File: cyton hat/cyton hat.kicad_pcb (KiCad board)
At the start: 4 copper layers, 61.4 x 61.3 mm, 59 parts, among them J1 Conn_02x13_Odd_Even, J2 Conn_01x08, J3 Conn_01x04, J4 Conn_01x02, J5 Conn_01x04, U1 ADS129x, U2 CP2102N-Axx-xQFN24

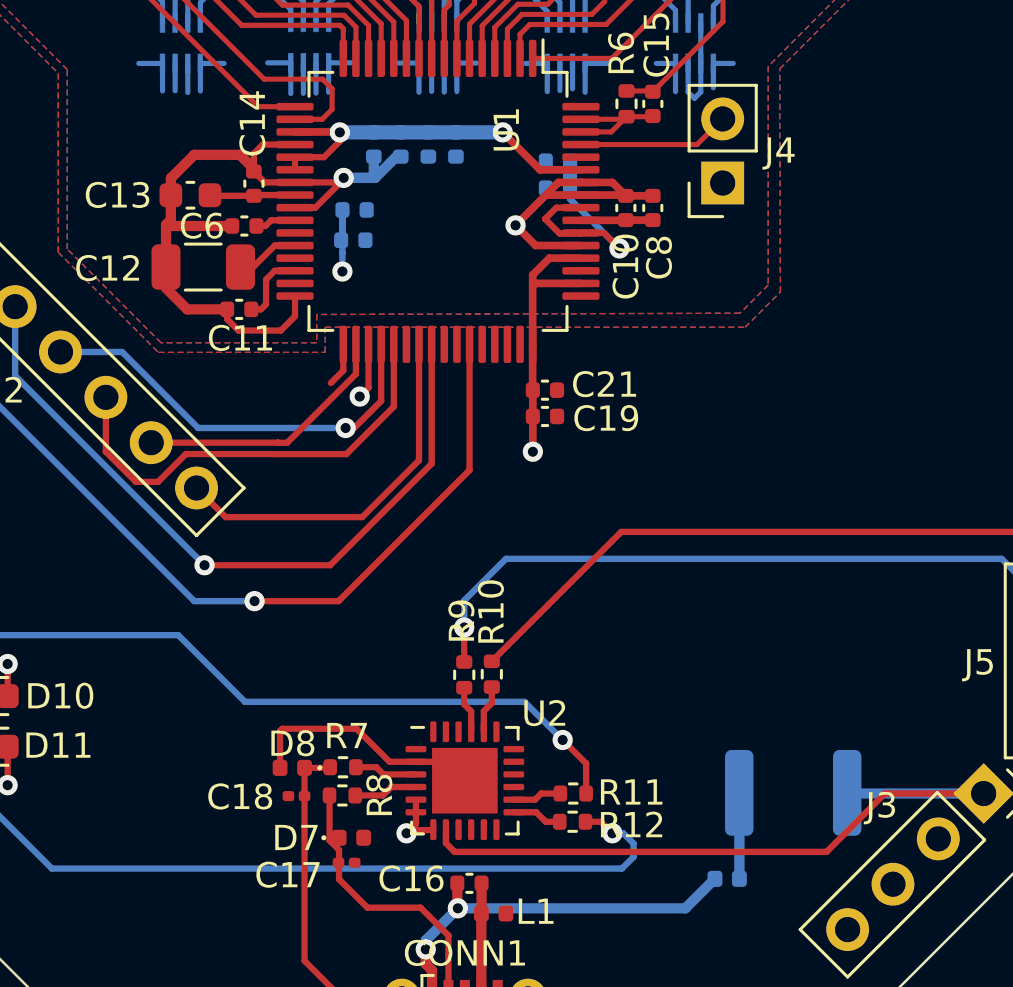
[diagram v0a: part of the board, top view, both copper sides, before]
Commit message: moved via that missed VSSA plane
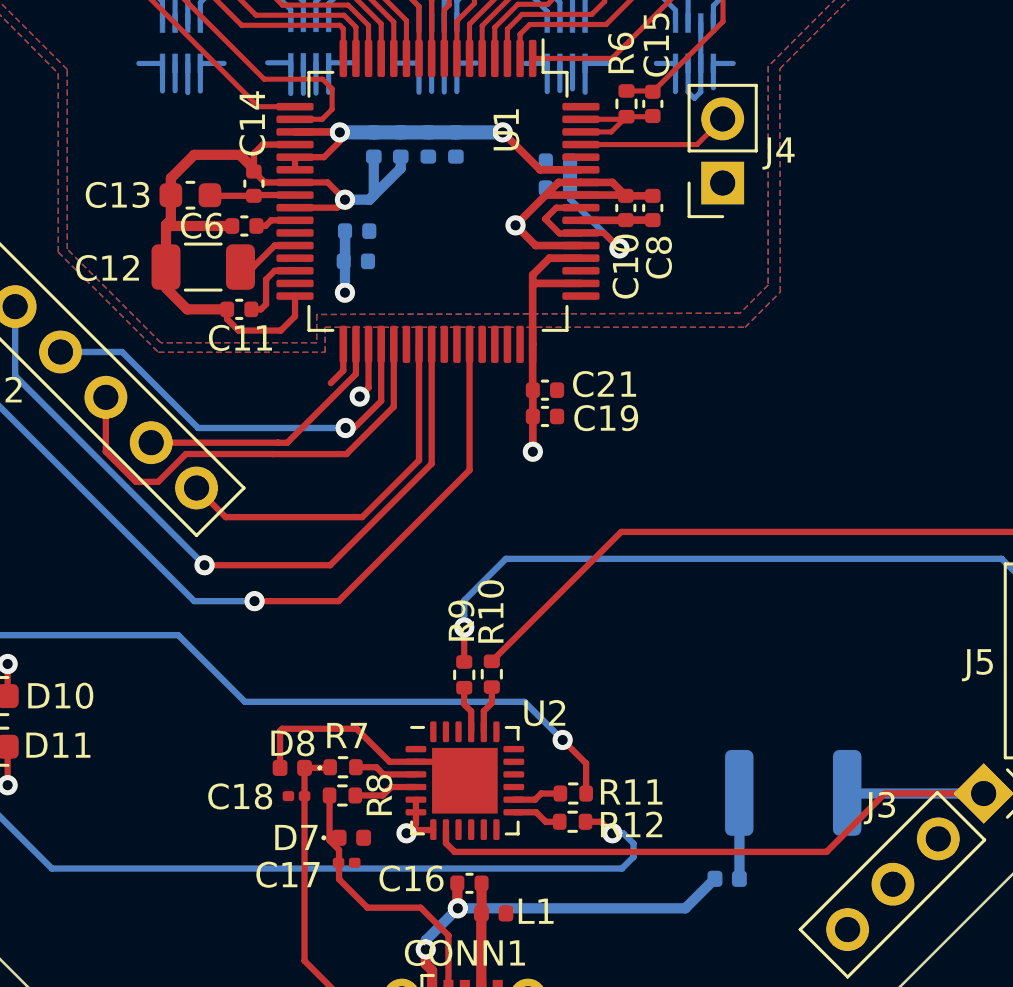
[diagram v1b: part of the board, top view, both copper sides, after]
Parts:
- moved C9 0.84 mm to (135.4, 104.2)
- moved C7 0.84 mm to (135.4, 103.0)
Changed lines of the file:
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@@
       (outputformat 1)
       (mirror false)
-      (drillshape 1)
+      (drillshape 0)
       (scaleselection 1)
-      (outputdirectory "")
+      (outputdirectory "plots/")
     )
   )
@@
     (fp_line (start -2 -1) (end -1 -2) (layer "F.Fab") (width 0.1))
     (fp_line (start -2 2) (end -2 -1) (layer "F.Fab") (width 0.1))
-    (pad "" smd roundrect (at 0.65 -0.65) (size 1.05 1.05) (layers "F.Paste") (roundrect_rratio 0.238095))
-    (pad "" smd roundrect (at -0.65 -0.65) (size 1.05 1.05) (layers "F.Paste") (roundrect_rratio 0.238095))
-    (pad "" smd roundrect (at -0.65 0.65) (size 1.05 1.05) (layers "F.Paste") (roundrect_rratio 0.238095))
-    (pad "" smd roundrect (at 0.65 0.65) (size 1.05 1.05) (layers "F.Paste") (roundrect_rratio 0.238095))
+    (pad "" smd roundrect (at 0.65 -0.65) (size 1.05 1.05) (layers "F.Paste") (roundrect_rratio 0.2380952381))
+    (pad "" smd roundrect (at -0.65 -0.65) (size 1.05 1.05) (layers "F.Paste") (roundrect_rratio 0.2380952381))
+    (pad "" smd roundrect (at -0.65 0.65) (size 1.05 1.05) (layers "F.Paste") (roundrect_rratio 0.2380952381))
+    (pad "" smd roundrect (at 0.65 0.65) (size 1.05 1.05) (layers "F.Paste") (roundrect_rratio 0.2380952381))
     (pad "1" smd roundrect (at -1.9375 -1.25) (size 0.825 0.25) (layers "F.Cu" "F.Paste" "F.Mask") (roundrect_rratio 0.25)
       (net 91 "unconnected-(U2-Pad1)") (pinfunction "~{RI}/CLK") (pintype "bidirectional+no_connect"))
@@
     (fp_line (start 1.6 0.8) (end -1.6 0.8) (layer "F.Fab") (width 0.1))
     (fp_line (start 1.6 -0.8) (end 1.6 0.8) (layer "F.Fab") (width 0.1))
-    (pad "1" smd roundrect (at -1.475 0) (size 1.15 1.8) (layers "F.Cu" "F.Paste" "F.Mask") (roundrect_rratio 0.217391)
+    (pad "1" smd roundrect (at -1.475 0) (size 1.15 1.8) (layers "F.Cu" "F.Paste" "F.Mask") (roundrect_rratio 0.2173913043)
       (net 21 "VSSA") (pintype "passive"))
-    (pad "2" smd roundrect (at 1.475 0) (size 1.15 1.8) (layers "F.Cu" "F.Paste" "F.Mask") (roundrect_rratio 0.217391)
+    (pad "2" smd roundrect (at 1.475 0) (size 1.15 1.8) (layers "F.Cu" "F.Paste" "F.Mask") (roundrect_rratio 0.2173913043)
       (net 25 "Net-(C12-Pad2)") (pintype "passive"))
     (model "${KICAD6_3DMODEL_DIR}/Capacitor_SMD.3dshapes/C_1206_3216Metric.wrl"
@@
     (fp_line (start -2.25 1.6) (end 2.25 1.6) (layer "B.Fab") (width 0.1))
     (fp_line (start 2.25 1.6) (end 2.25 -1.6) (layer "B.Fab") (width 0.1))
-    (pad "1" smd roundrect (at -2.1375 0 180) (size 1.125 3.4) (layers "B.Cu" "B.Paste" "B.Mask") (roundrect_rratio 0.222222)
+    (pad "1" smd roundrect (at -2.1375 0 180) (size 1.125 3.4) (layers "B.Cu" "B.Paste" "B.Mask") (roundrect_rratio 0.2222222222)
       (net 63 "VCOM") (pintype "passive"))
-    (pad "2" smd roundrect (at 2.1375 0 180) (size 1.125 3.4) (layers "B.Cu" "B.Paste" "B.Mask") (roundrect_rratio 0.222222)
+    (pad "2" smd roundrect (at 2.1375 0 180) (size 1.125 3.4) (layers "B.Cu" "B.Paste" "B.Mask") (roundrect_rratio 0.2222222222)
       (net 64 "Net-(F1-Pad2)") (pintype "passive"))
     (model "${KICAD6_3DMODEL_DIR}/Fuse.3dshapes/Fuse_1812_4532Metric.wrl"
@@
   )
   (footprint "Capacitor_SMD:C_0402_1005Metric" (layer "B.Cu")
-    (at 135.2804 103.406)
+    (at 135.382 104.2442)
     (descr "Capacitor SMD 0402 (1005 Metric), square (rectangular) end terminal, IPC_7351 nominal, (Body size source: IPC-SM-782 page 76, https://www.pcb-3d.com/wordpress/wp-content/uploads/ipc-sm-782a_amendment_1_and_2.pdf), generated with kicad-footprint-generator")
     (tags "capacitor")
@@
   )
   (footprint "Capacitor_SMD:C_0402_1005Metric" (layer "B.Cu")
-    (at 135.3312 102.2096)
+    (at 135.4328 103.0478)
     (descr "Capacitor SMD 0402 (1005 Metric), square (rectangular) end terminal, IPC_7351 nominal, (Body size source: IPC-SM-782 page 76, https://www.pcb-3d.com/wordpress/wp-content/uploads/ipc-sm-782a_amendment_1_and_2.pdf), generated with kicad-footprint-generator")
     (tags "capacitor")
@@
   (segment (start 131.699 99.6188) (end 131.3434 99.9744) (width 0.254) (layer "F.Cu") (net 21))
   (segment (start 145.5434 101.1188) (end 146.0754 101.6508) (width 0.3048) (layer "F.Cu") (net 21))
+  (segment (start 134.9502 101.8032) (end 134.6346 102.1188) (width 0.25) (layer "F.Cu") (net 21))
   (segment (start 146.0754 101.6508) (end 147.1422 101.6508) (width 0.3048) (layer "F.Cu") (net 21))
   (segment (start 127.915 102.8446) (end 127.8636 102.7932) (width 0.25) (layer "F.Cu") (net 21))
   (segment (start 128.0538 100.9526) (end 128.0538 101.6254) (width 0.4064) (layer "F.Cu") (net 21))
-  (segment (start 134.8994 100.994985) (end 133.775585 102.1188) (width 0.25) (layer "F.Cu") (net 21))
   (segment (start 144.2974 101.6188) (end 146.0434 101.6188) (width 0.3048) (layer "F.Cu") (net 21))
   (segment (start 146.0434 101.6188) (end 146.0754 101.6508) (width 0.2032) (layer "F.Cu") (net 21))
@@
   (segment (start 131.3434 99.9744) (end 131.3434 100.6882) (width 0.254) (layer "F.Cu") (net 21))
   (segment (start 131.774 101.1188) (end 131.3434 100.6882) (width 0.254) (layer "F.Cu") (net 21))
-  (segment (start 134.8994 100.9396) (end 134.7202 101.1188) (width 0.25) (layer "F.Cu") (net 21))
-  (segment (start 134.7202 101.1188) (end 132.9724 101.1188) (width 0.25) (layer "F.Cu") (net 21))
   (segment (start 128.0538 101.6254) (end 128.0538 102.603) (width 0.4064) (layer "F.Cu") (net 21))
   (segment (start 130.2818 106.5328) (end 130.2818 106.1466) (width 0.25) (layer "F.Cu") (net 21))
-  (segment (start 133.775585 102.1188) (end 132.9724 102.1188) (width 0.25) (layer "F.Cu") (net 21))
+  (segment (start 134.9502 101.8032) (end 134.2658 101.1188) (width 0.25) (layer "F.Cu") (net 21))
   (segment (start 132.9724 101.1188) (end 131.774 101.1188) (width 0.254) (layer "F.Cu") (net 21))
   (segment (start 127.8636 104.4684) (end 127.8618 104.4702) (width 0.25) (layer "F.Cu") (net 21))
@@
   (segment (start 144.2974 101.6188) (end 142.9192 101.6188) (width 0.3048) (layer "F.Cu") (net 21))
   (segment (start 143.407 101.1188) (end 142.9131 101.6127) (width 0.3048) (layer "F.Cu") (net 21))
-  (segment (start 134.8994 100.9396) (end 134.8994 100.994985) (width 0.25) (layer "F.Cu") (net 21))
+  (segment (start 134.2658 101.1188) (end 132.9724 101.1188) (width 0.25) (layer "F.Cu") (net 21))
+  (segment (start 134.6346 102.1188) (end 132.9724 102.1188) (width 0.25) (layer "F.Cu") (net 21))
   (segment (start 142.5062 103.6188) (end 141.7066 102.8192) (width 0.3048) (layer "F.Cu") (net 21))
   (segment (start 130.7846 100.0252) (end 128.9812 100.0252) (width 0.4064) (layer "F.Cu") (net 21))
@@
   (segment (start 127.8636 102.7932) (end 127.8636 104.4684) (width 0.4064) (layer "F.Cu") (net 21))
   (segment (start 132.9724 105.6188) (end 132.9724 106.4226) (width 0.25) (layer "F.Cu") (net 21))
-  (via (at 134.8994 100.9396) (size 0.8) (drill 0.4) (layers "F.Cu" "B.Cu") (net 21))
-  (via (at 134.8486 104.648) (size 0.8) (drill 0.4) (layers "F.Cu" "B.Cu") (free) (net 21))
+  (via (at 134.9502 101.8032) (size 0.8) (drill 0.4) (layers "F.Cu" "B.Cu") (net 21))
+  (via (at 134.9502 105.4862) (size 0.8) (drill 0.4) (layers "F.Cu" "B.Cu") (free) (net 21))
   (via (at 141.7066 102.8192) (size 0.8) (drill 0.4) (layers "F.Cu" "B.Cu") (net 21))
-  (segment (start 134.8486 104.648) (end 134.8486 103.9042) (width 0.25) (layer "B.Cu") (net 21))
-  (segment (start 134.8512 103.9016) (end 134.8512 102.2096) (width 0.25) (layer "B.Cu") (net 21))
-  (segment (start 134.8486 103.9042) (end 134.8512 103.9016) (width 0.25) (layer "B.Cu") (net 21))
+  (segment (start 134.9502 105.4862) (end 134.9502 104.7424) (width 0.4064) (layer "B.Cu") (net 21))
+  (segment (start 135.9154 101.8032) (end 137.16 100.5586) (width 0.4064) (layer "B.Cu") (net 21))
+  (segment (start 136.0932 100.0962) (end 136.0932 101.6254) (width 0.4064) (layer "B.Cu") (net 21))
+  (segment (start 137.16 100.5586) (end 137.16 100.0962) (width 0.4064) (layer "B.Cu") (net 21))
+  (segment (start 134.9528 104.7398) (end 134.9528 103.0478) (width 0.4064) (layer "B.Cu") (net 21))
+  (segment (start 134.9502 104.7424) (end 134.9528 104.7398) (width 0.25) (layer "B.Cu") (net 21))
   (segment (start 126.176799 89.143599) (end 127.33655 89.143599) (width 0.2032) (layer "B.Cu") (net 21))
-  (segment (start 137.16 100.0962) (end 136.9874 100.0962) (width 0.25) (layer "B.Cu") (net 21))
-  (segment (start 136.0932 100.0962) (end 136.0932 100.7618) (width 0.4064) (layer "B.Cu") (net 21))
-  (segment (start 136.144 100.9396) (end 134.8994 100.9396) (width 0.4064) (layer "B.Cu") (net 21))
-  (segment (start 134.8512 103.3552) (end 134.8004 103.406) (width 0.25) (layer "B.Cu") (net 21))
+  (segment (start 134.9528 104.1934) (end 134.902 104.2442) (width 0.25) (layer "B.Cu") (net 21))
   (segment (start 124.6632 84.9884) (end 124.6632 87.63) (width 0.2032) (layer "B.Cu") (net 21))
-  (segment (start 136.0932 100.7618) (end 135.9154 100.9396) (width 0.25) (layer "B.Cu") (net 21))
-  (segment (start 135.9154 100.9396) (end 134.8994 100.9396) (width 0.4064) (layer "B.Cu") (net 21))
-  (segment (start 136.9874 100.0962) (end 136.144 100.9396) (width 0.4064) (layer "B.Cu") (net 21))
+  (segment (start 134.9502 101.8032) (end 135.9154 101.8032) (width 0.4064) (layer "B.Cu") (net 21))
+  (segment (start 136.0932 101.6254) (end 135.9154 101.8032) (width 0.4064) (layer "B.Cu") (net 21))
   (segment (start 124.6632 87.63) (end 126.176799 89.143599) (width 0.2032) (layer "B.Cu") (net 21))
-  (segment (start 134.8512 102.2096) (end 134.8512 103.3552) (width 0.25) (layer "B.Cu") (net 21))
+  (segment (start 134.9528 103.0478) (end 134.9528 104.1934) (width 0.4064) (layer "B.Cu") (net 21))
   (segment (start 132.0264 102.6188) (end 132.9724 102.6188) (width 0.25) (layer "F.Cu") (net 22))
   (segment (start 131.8006 102.8446) (end 132.0264 102.6188) (width 0.25) (layer "F.Cu") (net 22))

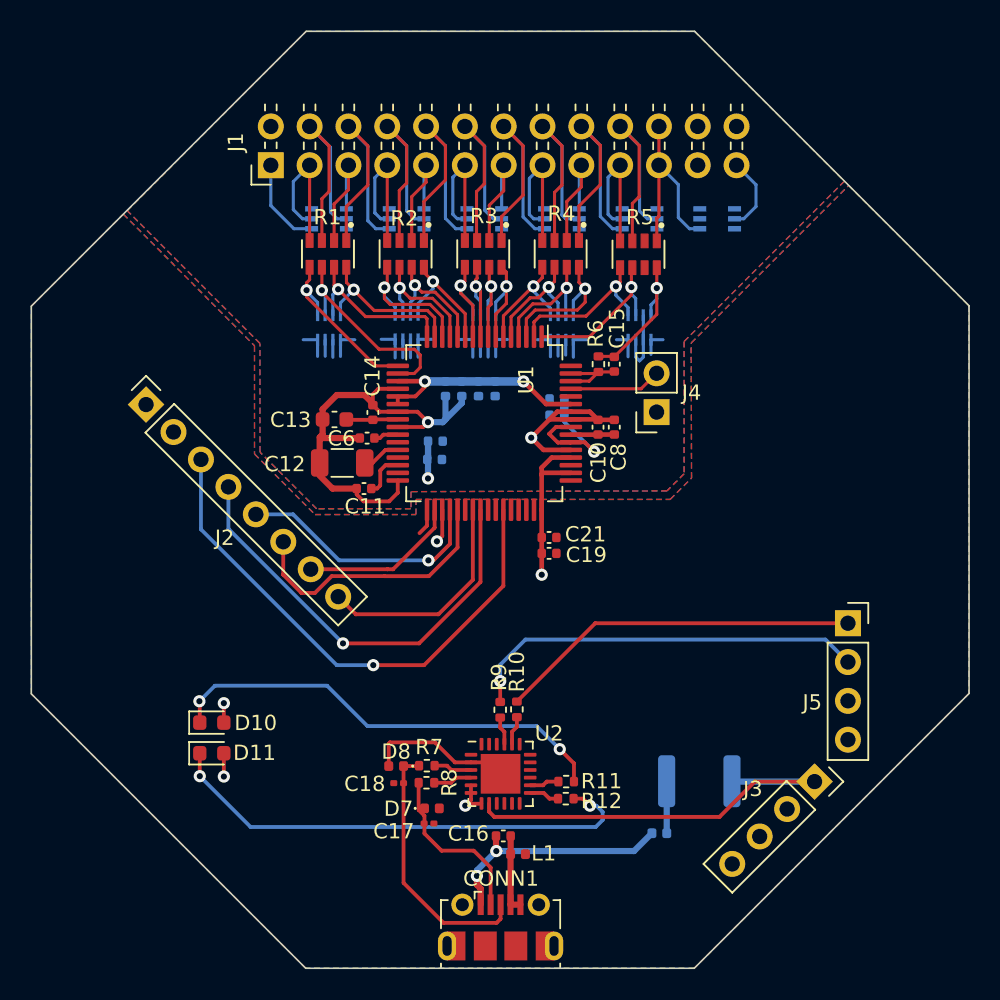
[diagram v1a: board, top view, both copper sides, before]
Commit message: fixed D9 footprint problem
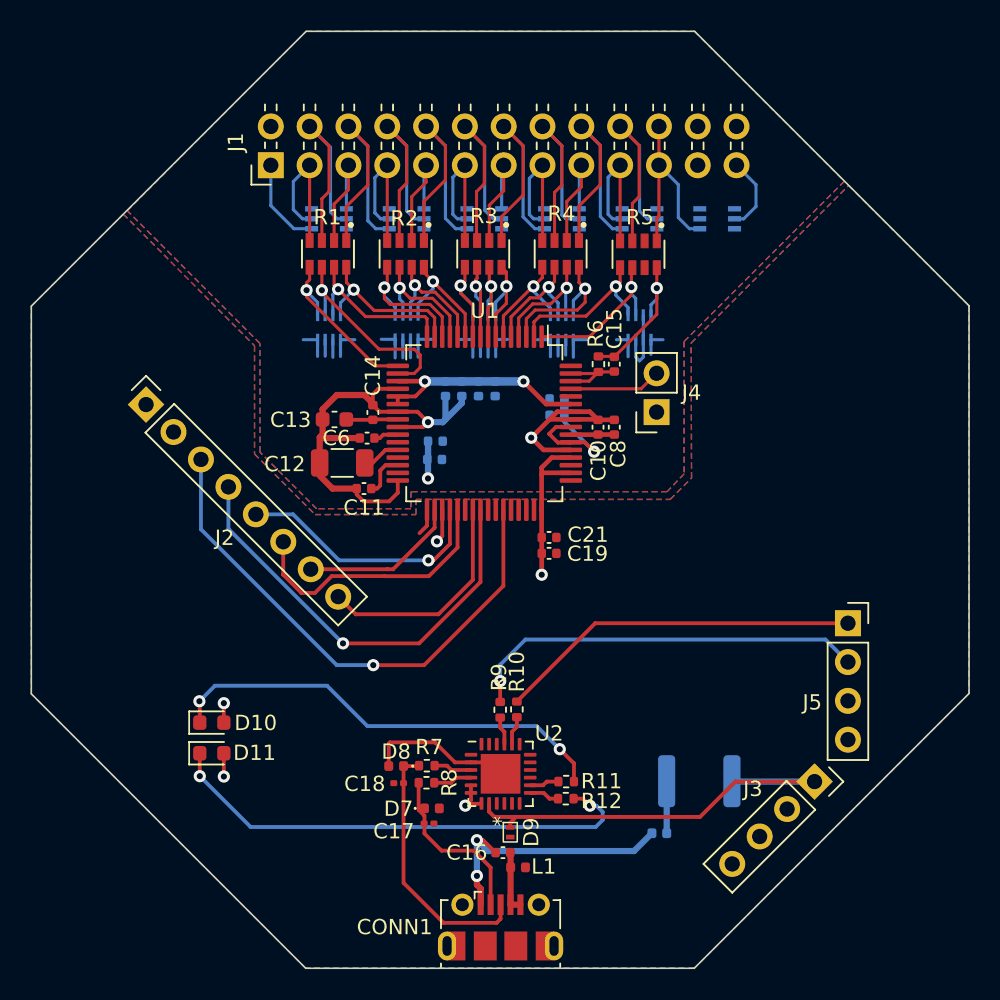
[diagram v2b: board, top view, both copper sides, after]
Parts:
- added D9: TVS_D, TSV - Diodes:ESDALC6V1-1M2, F.Cu at (140.3, 128.6)
- D1, D2, D3, D4, D5, D6: value DCK6_TEX -> TPD4E1B06DCKR
- moved C16 1.09 mm to (139.9, 130.0)
- moved L1 0.86 mm to (140.8, 130.9)
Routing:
- net Net-(C16-Pad1): track 15.8 -> 18.1 mm
- net VCOM: track 28.4 -> 29.6 mm
- net Net-(C16-Pad2): track 5.16 -> 5.79 mm

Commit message: updated gerbers
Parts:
- added REF**: Fiducial_1mm_Mask2mm, Fiducial:Fiducial_1mm_Mask2mm, F.Cu at (165.0, 96.0)
- added REF**: Fiducial_1mm_Mask2mm, Fiducial:Fiducial_1mm_Mask2mm, F.Cu at (128.7, 133.5)
- added REF**: Fiducial_1mm_Mask2mm, Fiducial:Fiducial_1mm_Mask2mm, F.Cu at (113.1, 96.2)
- added REF**: Fiducial_1mm_Mask2mm, Fiducial:Fiducial_1mm_Mask2mm, B.Cu at (128.7, 133.5)
- added REF**: Fiducial_1mm_Mask2mm, Fiducial:Fiducial_1mm_Mask2mm, B.Cu at (165.0, 96.0)
- added REF**: Fiducial_1mm_Mask2mm, Fiducial:Fiducial_1mm_Mask2mm, B.Cu at (113.1, 96.2)
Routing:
- net /TXD: track 26.5 -> 24.7 mm
- net Net-(C16-Pad1): track 18.1 -> 16.6 mm
- net Net-(D11-Pad1): track 32.2 -> 30.9 mm
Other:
- outline, holes or cut-outs redrawn
- board text added: "BRAIN-4CE"
- board text added: "CYTON HAT V1"
